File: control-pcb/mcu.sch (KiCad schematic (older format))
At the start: 28 parts, among them P5 CONN_01X02, Q8 2N7002, SW2 SW_PUSH, U5 STM32F072CB, U6 24AA01, Y1 8kHz

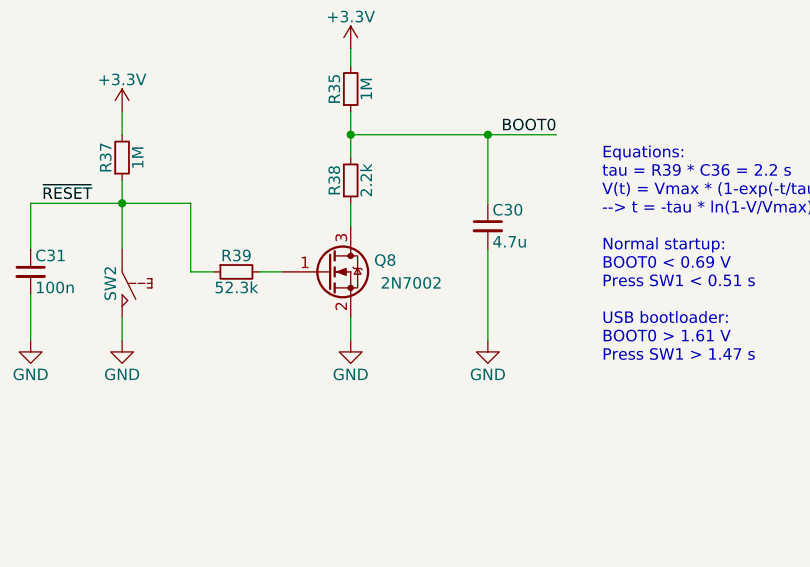
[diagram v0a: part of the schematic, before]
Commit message: Issues #1, #2 and #4 fixed
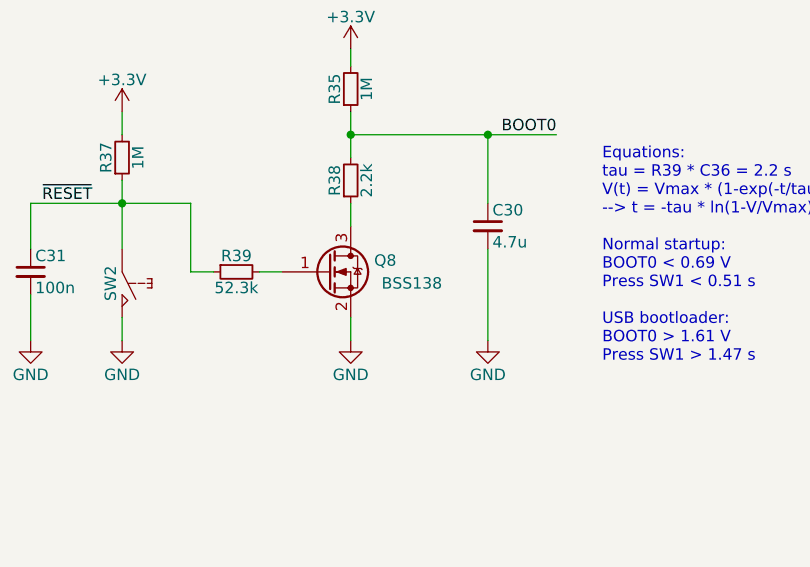
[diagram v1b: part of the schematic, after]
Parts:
- Q8: value 2N7002 -> BSS138; Manufacturer Nexperia -> Fairchild Semiconductor; PartNumber 2N7002,215 -> BSS138
- U6: PartNumber 24AA01 -> 24AA01T-I/OT
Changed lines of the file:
@@
 EESchema Schematic File Version 2
-LIBS:BMS-5s-rescue
 LIBS:IEC-60617
 LIBS:LibreSolar
@@
 F 3 "" H -100 350 60  0000 C CNN
 F 4 "Microchip" H 0   0   60  0001 C CNN "Manufacturer"
-F 5 "24AA01" H 0   0   60  0001 C CNN "PartNumber"
+F 5 "24AA01T-I/OT" H 0   0   60  0001 C CNN "PartNumber"
 	1    2400 6500
 	1    0    0    -1
@@
 P 8400 2900
 F 0 "Q8" H 8700 2950 50  0000 R CNN
-F 1 "2N7002" H 8900 2850 50  0000 R CNN
+F 1 "BSS138" H 8900 2850 50  0000 R CNN
 F 2 "LibreSolar:SOT-23" H 8600 3000 50  0001 C CNN
 F 3 "" H 8400 2900 50  0000 C CNN
-F 4 "Nexperia" H 8400 2900 60  0001 C CNN "Manufacturer"
-F 5 "2N7002,215" H 8400 2900 60  0001 C CNN "PartNumber"
+F 4 "Fairchild Semiconductor" H 8400 2900 60  0001 C CNN "Manufacturer"
+F 5 "BSS138" H 8400 2900 60  0001 C CNN "PartNumber"
 	1    8400 2900
 	1    0    0    -1

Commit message: Update to KiCAD 5 and minor changes in part selection
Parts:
- C27, C31, C32, C33, C34, C36: symbol C -> Project:C; Manufacturer Murata -> Yageo; PartNumber GRM188R71H104KA93D -> CC0603KRX7R9BB104
- C30, C35: symbol C -> Project:C
- D17: symbol LM4040 -> Project:LM4040
- L3: symbol L -> Project:L
- LED1, LED2: footprint LEDs:LED_D3.0mm -> LED_THT:LED_D3.0mm; symbol LED -> Project:D_LED
- LED3, LED4: footprint LEDs:LED_0603 -> LED_SMD:LED_0603_1608Metric; symbol LED -> Project:D_LED
- P5: footprint Pin_Headers:Pin_Header_Straight_1x02_Pitch2.54mm -> Connector_PinHeader_2.54mm:PinHeader_1x02_P2.54mm_Vertical; symbol CONN_01X02 -> Project:Conn_01x02
- Q8: symbol Q_NMOS_GSD -> Project:Q_NMOS_GSD
- R35, R37, R38, R39, R40, R41, R42: symbol R -> Project:R
- SW2: symbol SW_PUSH -> Project:SW_PUSH
- SWD1: footprint Pin_Headers:Pin_Header_Straight_1x06_Pitch2.54mm -> Connector_PinHeader_2.54mm:PinHeader_1x06_P2.54mm_Vertical; symbol ST_Nucleo_SWD -> LibreSolar:ST_Nucleo_SWD
- U5: footprint Housings_QFP:LQFP-48_7x7mm_Pitch0.5mm -> Package_QFP:LQFP-48_7x7mm_P0.5mm; symbol STM32F072CB -> LibreSolar:STM32F072CB
- U6: footprint TO_SOT_Packages_SMD:SOT-23-5 -> LibreSolar:SOT-23-5; symbol 24AA01 -> LibreSolar:24AA01
- Y1: footprint LibreSolar:Resonator_Murata_CSTCE -> LibreSolar:Resonator_Murata_CSTCE_G; symbol Resonator -> Project:Resonator
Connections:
- wire segments 117 -> 137
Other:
- moved on the sheet: Y1
